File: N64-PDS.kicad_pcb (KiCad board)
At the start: 2 copper layers, 36 x 59.8 mm, 40 parts, among them J1 PWR_OUT, J2 I2C_OUT, J3 USB-C-6P-PWR, U1 ST1S41PHR, U2 ST1S41PHR, U3 STL6P3LLH6, U4 STUSB4500QTR

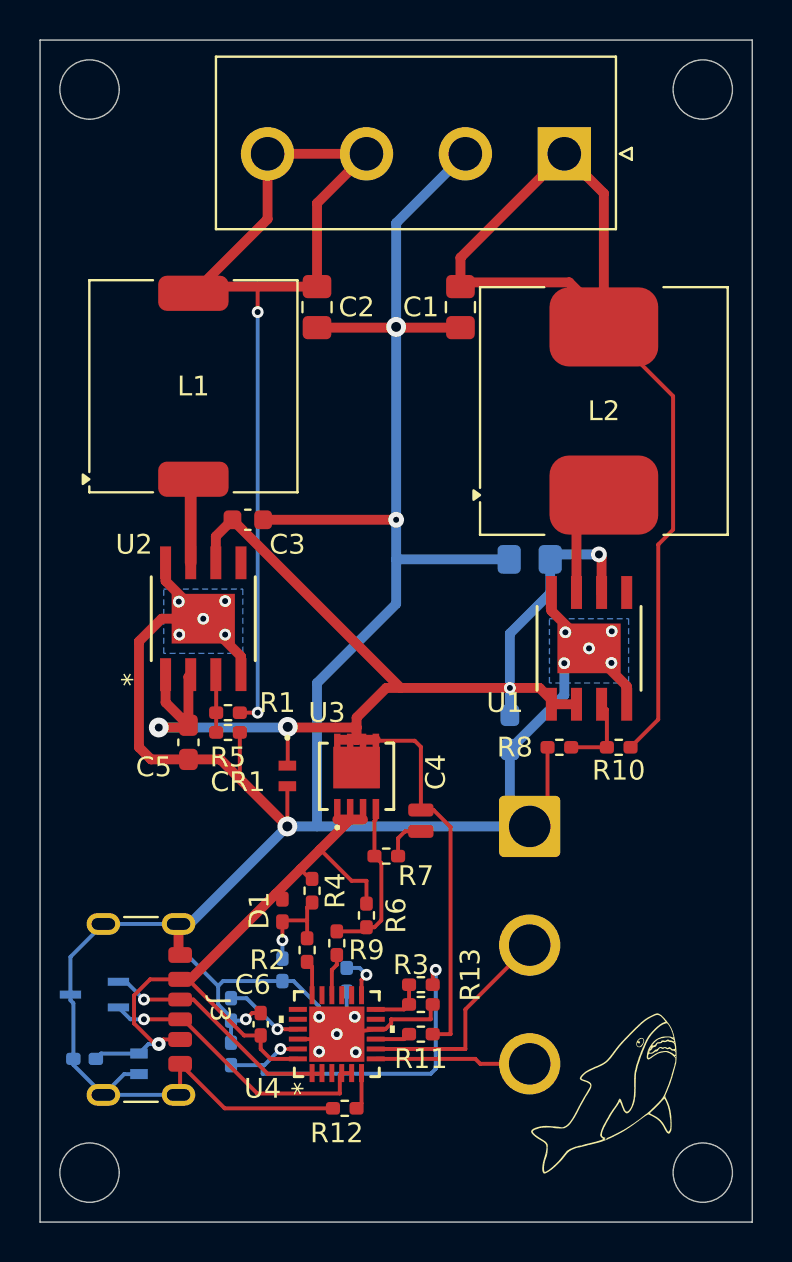
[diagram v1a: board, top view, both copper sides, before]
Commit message: Update PCB
slight reshuffle of the PCB in the aim of reducing noise from smps
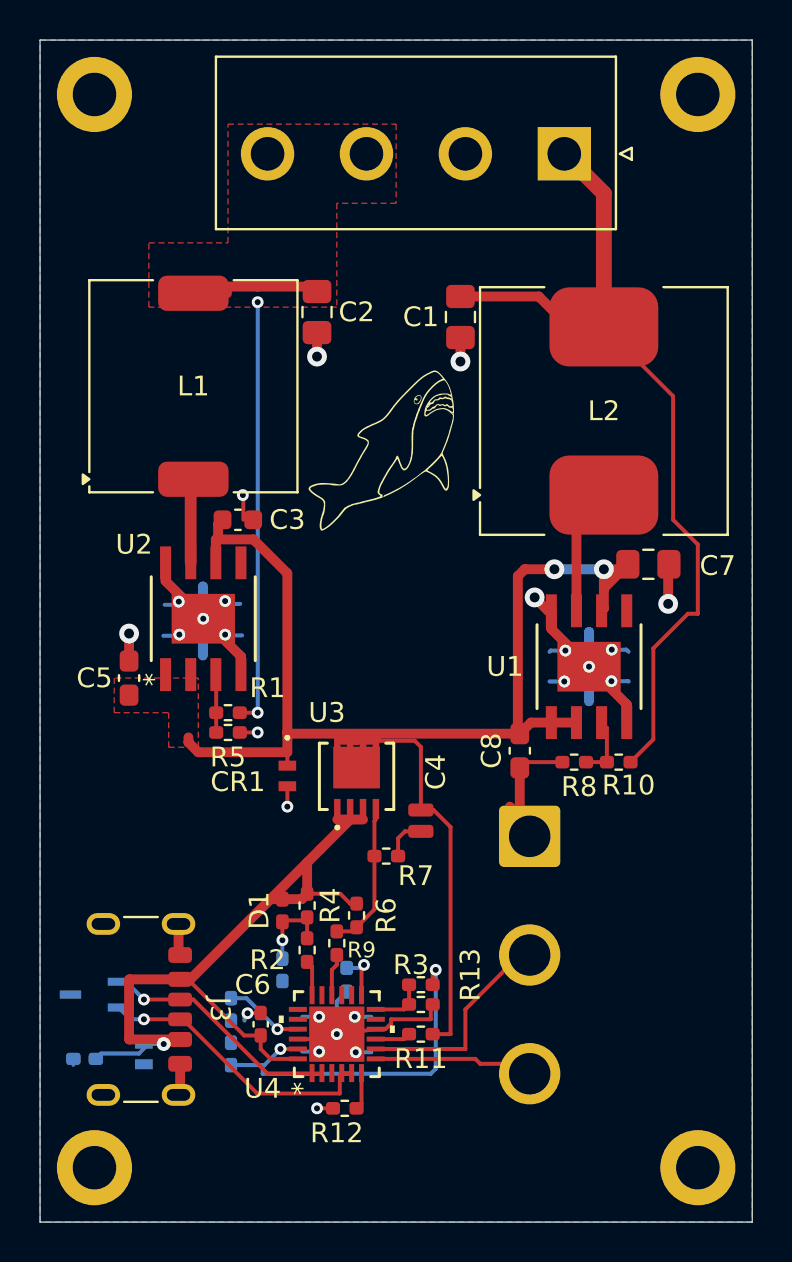
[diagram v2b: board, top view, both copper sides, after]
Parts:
- added REF**: MountingHole_2.2mm_M2_DIN965_Pad, MountingHole:MountingHole_2.2mm_M2_DIN965_Pad, F.Cu at (166.8, 68.5)
- added REF**: MountingHole_2.2mm_M2_DIN965_Pad, MountingHole:MountingHole_2.2mm_M2_DIN965_Pad, F.Cu at (166.8, 122.8)
- added REF**: MountingHole_2.2mm_M2_DIN965_Pad, MountingHole:MountingHole_2.2mm_M2_DIN965_Pad, F.Cu at (136.2, 122.8)
- added REF**: MountingHole_2.2mm_M2_DIN965_Pad, MountingHole:MountingHole_2.2mm_M2_DIN965_Pad, F.Cu at (136.2, 68.5)
- C7, C8: moved to F.Cu
- moved G*** 34.4 mm to (150.8, 86.5)
- moved C7 6.01 mm to (164.2, 92.2), turned to 0 degrees
- moved C5 4.42 mm to (138.0, 98.0), turned to -90 degrees
- moved R8 1.06 mm to (160.5, 102.2)
- moved C8 1.05 mm to (157.8, 101.7)
- moved U1 0.92 mm to (161.2, 97.4)
- moved R4 0.79 mm to (147.0, 109.5)
- moved R10 0.75 mm to (162.8, 102.2)
- moved CR3 0.56 mm to (138.8, 117.0)
- moved C1 0.50 mm to (154.8, 79.8)
- moved C3 0.50 mm to (143.5, 90.0)
- moved J2 0.50 mm to (158.2, 106.0)
- moved R6 0.50 mm to (149.5, 110.0)
- moved C2 0.25 mm to (147.5, 79.5)
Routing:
- net GND: track 183.3 -> 65.3 mm, vias 19 -> 25
- net 3V3O: track 49.7 -> 29.3 mm
- net 12VO: track 49.8 -> 41.4 mm
- net VSNK: track 81.8 -> 75.8 mm, vias 4 -> 2
- net /VBUS: track 36.5 -> 40.0 mm
- net /12V_SWO: track 3.54 -> 5.92 mm
- net /VBUS_VS_DISCH: track 4.95 -> 3.94 mm
- net 12VFB: track 4.09 -> 3.17 mm
- net Net-(U3-G): track 7.46 -> 6.94 mm
- added copper zone on F.Cu, net 3V3O
- added copper zone on F.Cu, net VSNK
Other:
- outline, holes or cut-outs redrawn

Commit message: Re-route
Re-route to improve design, further updates to come
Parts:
- C10, C11, CR2, CR3: moved to F.Cu
- C12: footprint Capacitor_SMD:C_0402_1005Metric_Pad0.74x0.62mm_HandSolder -> Capacitor_SMD:C_0805_2012Metric_Pad1.18x1.45mm_HandSolder; moved to F.Cu
- moved C12 12.0 mm to (144.5, 109.0)
- moved CR2 8.03 mm to (144.2, 115.0), turned to 0 degrees
- moved CR3 7.28 mm to (143.5, 111.5), turned to 90 degrees
- moved J2 6.75 mm to (165.0, 106.0)
- moved R12 5.25 mm to (154.0, 121.0), turned to 90 degrees
- moved C11 5.01 mm to (148.0, 116.0), turned to 180 degrees
- moved C10 4.85 mm to (148.0, 117.0), turned to 180 degrees
- moved C6 4.53 mm to (148.4, 118.0), turned to 180 degrees
- moved C9 4.09 mm to (149.8, 113.6)
- moved D1 4.09 mm to (149.8, 110.6)
- moved R11 4.09 mm to (156.8, 116.8)
- moved R13 4.09 mm to (156.8, 115.3)
- moved R14 4.09 mm to (153.0, 114.1)
- moved R2 4.09 mm to (151.0, 112.6)
- moved R3 4.09 mm to (156.8, 114.3)
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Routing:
- net GND: track 65.3 -> 86.4 mm, vias 25 -> 26
- net 2V7: track 18.8 -> 12.7 mm
- net /VBUS: track 40.0 -> 43.0 mm, vias 1 -> 2
- net /I2C_SDA: track 11.1 -> 14.0 mm
- net Net-(U3-G): track 6.94 -> 9.77 mm
- net Net-(J3-CC1): track 11.8 -> 14.6 mm, vias 1 -> 2
- net /I2C_SCL: track 7.89 -> 10.6 mm
- net VSNK: track 75.8 -> 78.4 mm
- net Net-(J3-CC2): track 14.4 -> 16.7 mm, vias 1 -> 2
- net Net-(U4-VREG_1V2): track 4.03 -> 2.21 mm, vias 1 -> 0
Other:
- board size 36 x 59.8 mm -> 35.5 x 59.8 mm

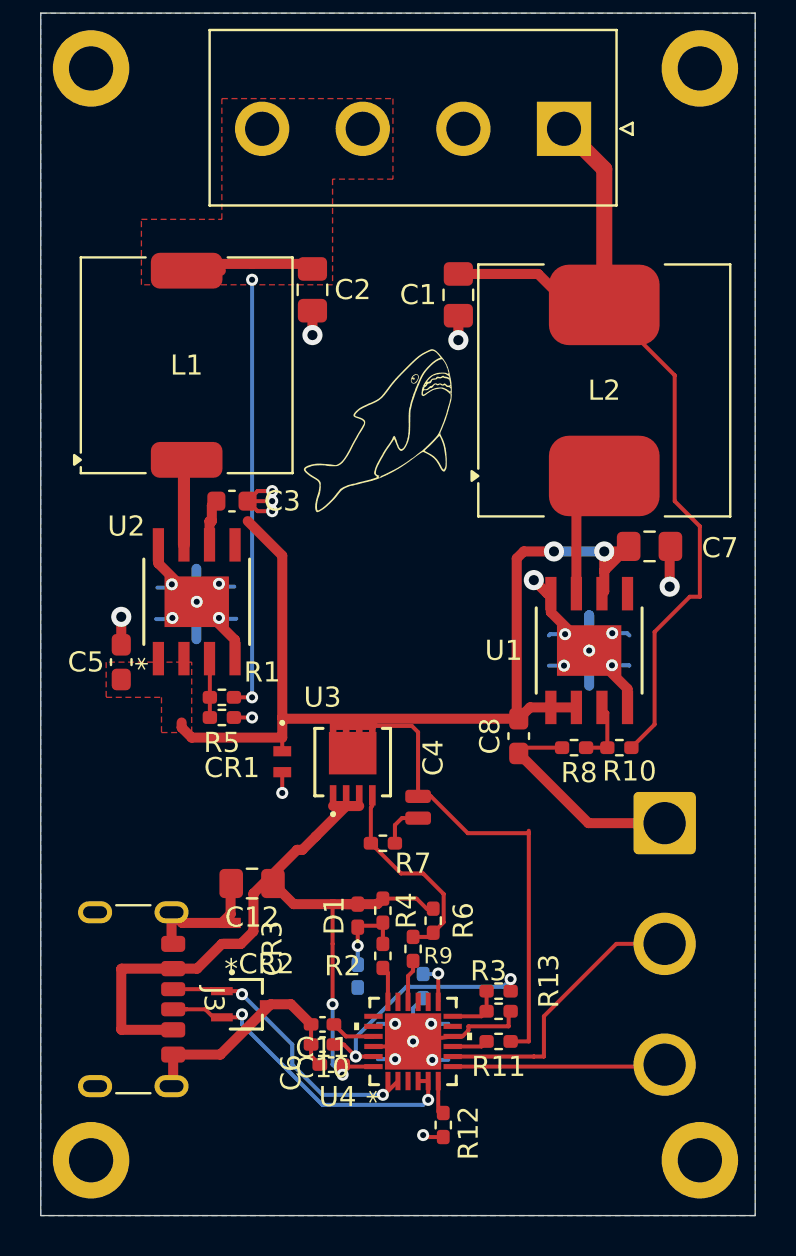
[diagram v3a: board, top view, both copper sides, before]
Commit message: 4Layer
4 layer board, destroy 12v rail to make space for new 12v rail.
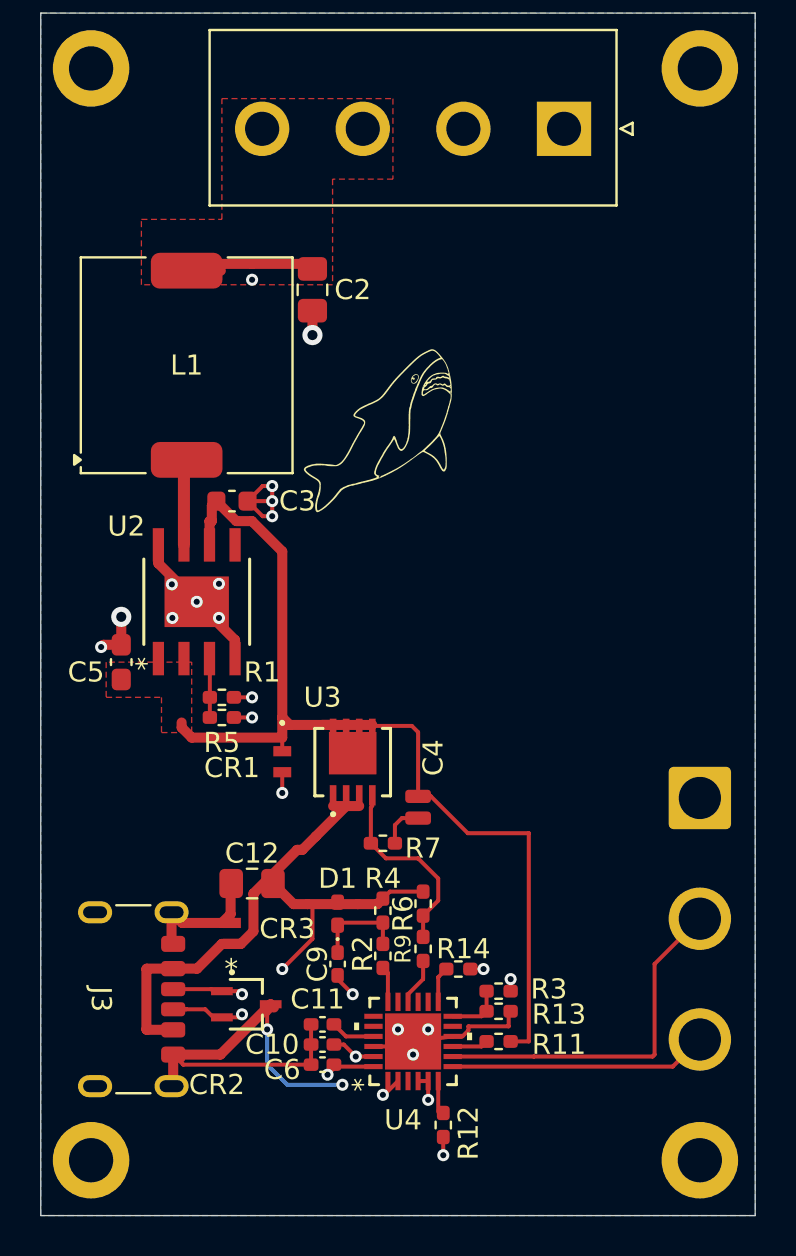
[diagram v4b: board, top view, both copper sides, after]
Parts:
- removed C1, C7: 10u, Capacitor_SMD:C_0805_2012Metric_Pad1.18x1.45mm_HandSolder
- removed C8: 10u, Capacitor_SMD:C_0603_1608Metric_Pad1.08x0.95mm_HandSolder
- removed L2: 10u, Inductor_SMD:L_Coilcraft_MSS1260-XXX
- removed R10: 180k, Resistor_SMD:R_0402_1005Metric_Pad0.72x0.64mm_HandSolder
- removed R8: 13k, Resistor_SMD:R_0402_1005Metric_Pad0.72x0.64mm_HandSolder
- removed U1: ST1S41PHR, ST1S41PHR:HSOP8_STM-M
- C9, R14: moved to F.Cu
- moved J2 2.15 mm to (166.8, 104.8)
- moved R14 1.94 mm to (154.8, 113.2), turned to 0 degrees
- moved C9 1.16 mm to (148.8, 113.0)
- moved D1 1.00 mm to (148.8, 110.5)
- moved R6 0.98 mm to (153.0, 110.0)
- moved R9 0.50 mm to (153.0, 112.2)
- moved C6 0.43 mm to (148.0, 118.0)
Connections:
- REF** pad 1: (no net) -> GND
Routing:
- net 12VO: track 41.4 -> 0.00 mm
- net VSNK: track 78.4 -> 50.4 mm, vias 2 -> 0
- net GND: track 86.4 -> 58.7 mm, vias 26 -> 21
- net /12V_SWO: track 5.92 -> 0.00 mm
- net /I2C_SDA: track 14.0 -> 17.8 mm
- net 12VFB: track 3.17 -> 0.00 mm
- net /I2C_SCL: track 10.6 -> 12.8 mm
- net /VBUS: track 43.0 -> 41.4 mm
- net Net-(J3-CC1): track 14.6 -> 15.7 mm
- net Net-(J3-CC2): track 16.7 -> 17.9 mm
- net /VBUS_VS_DISCH: track 3.94 -> 4.57 mm, vias 1 -> 0
- net Net-(U3-G): track 9.77 -> 9.16 mm
- net /ADDR1: track 2.17 -> 1.80 mm, vias 1 -> 0
- added copper zone on In1.Cu, net GND
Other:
- copper layers 2 -> 4

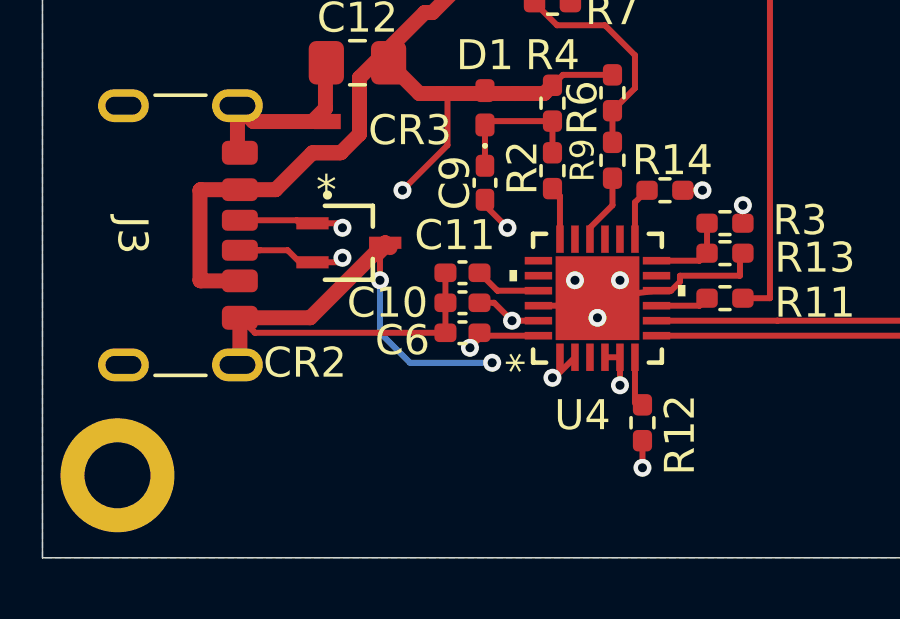
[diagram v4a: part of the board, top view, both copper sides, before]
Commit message: Component switch
Switch buck/boost converter components, Complete schematic
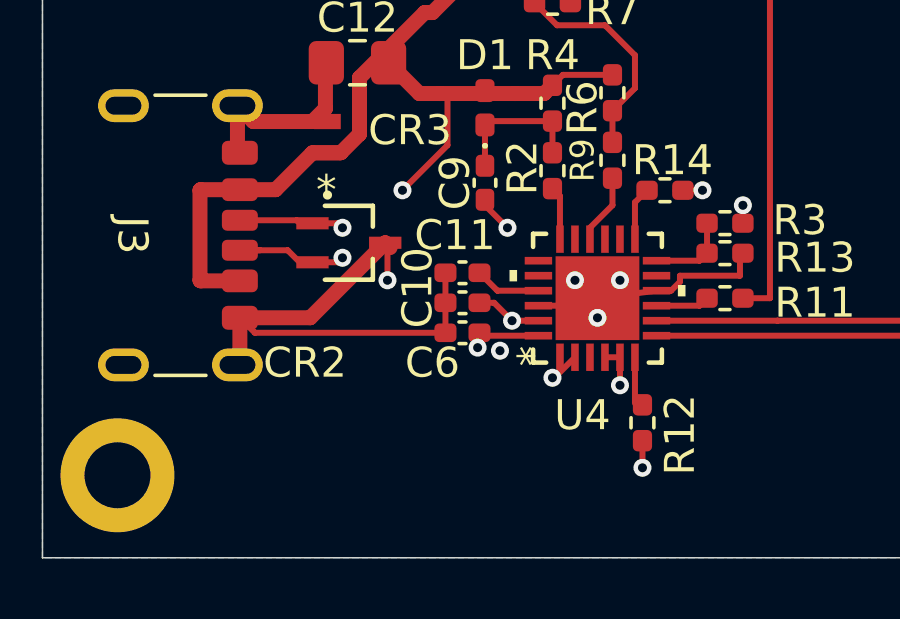
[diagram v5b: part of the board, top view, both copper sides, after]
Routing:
- net GND: track 58.7 -> 59.9 mm
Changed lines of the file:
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@@
 		(tags "capacitor handsolder")
 		(property "Reference" "C10"
-			(at 2.5 0 0)
+			(at 1.5 0.5 90)
 			(layer "F.SilkS")
 			(effects
@@
 		(tags "capacitor handsolder")
 		(property "Reference" "C6"
-			(at 2 -0.25 180)
+			(at 1 -1 180)
 			(layer "F.SilkS")
 			(effects
@@
 		)
 		(fp_text user "*"
-			(at -2.1525 -2.5 90)
+			(at -1.92802 -2.1463 90)
 			(unlocked yes)
 			(layer "F.SilkS")
@@
 	)
 	(segment
-		(start 148.5675 118.1825)
-		(end 148.25 118.5)
-		(width 0.2)
-		(layer "F.Cu")
-		(net 2)
-	)
-	(segment
 		(start 151 109.75)
 		(end 150.725 110.025)
@@
 	)
 	(segment
-		(start 148.5675 118)
-		(end 148.5675 118.1825)
-		(width 0.2)
-		(layer "F.Cu")
-		(net 2)
-	)
-	(segment
 		(start 149.75 110.025)
 		(end 148.5 110.025)
@@
 	)
 	(segment
+		(start 148.505232 118.494923)
+		(end 148.5675 118.432655)
+		(width 0.2)
+		(layer "F.Cu")
+		(net 2)
+	)
+	(segment
 		(start 147 107.325998)
 		(end 146.741502 107.325998)
@@
 	)
 	(segment
+		(start 148.5675 118.432655)
+		(end 148.5675 118)
+		(width 0.2)
+		(layer "F.Cu")
+		(net 2)
+	)
+	(segment
 		(start 147.662999 106.662999)
 		(end 149.174999 105.151)
@@
 	)
 	(via
-		(at 148.25 118.5)
+		(at 148.505232 118.494923)
 		(size 0.6)
 		(drill 0.3)
@@
 	)
 	(segment
-		(start 147.5 117.75)
-		(end 147.5 114.75)
+		(start 147.5 114.75)
+		(end 146 113.25)
 		(width 0.2)
 		(layer "In2.Cu")
@@
 	)
 	(segment
-		(start 148.25 118.5)
-		(end 147.5 117.75)
+		(start 148.505232 118.494923)
+		(end 147.5 117.489691)
 		(width 0.2)
 		(layer "In2.Cu")
@@
 	)
 	(segment
-		(start 147.5 114.75)
-		(end 146 113.25)
+		(start 147.5 117.489691)
+		(end 147.5 114.75)
 		(width 0.2)
 		(layer "In2.Cu")
@@
 	)
 	(segment
+		(start 142.9257 117.5)
+		(end 140.58 117.5)
+		(width 0.5)
+		(layer "F.Cu")
+		(net 3)
+	)
+	(segment
 		(start 140.5 110.43)
 		(end 140.5 111.92)
@@
 	)
 	(segment
-		(start 145.25 115.5)
-		(end 145.25 116.25)
+		(start 145.5 115.25)
+		(end 145.58785 115.16215)
 		(width 0.2)
 		(layer "F.Cu")
@@
 	)
 	(segment
-		(start 145.4257 115)
-		(end 142.9257 117.5)
-		(width 0.5)
-		(layer "F.Cu")
-		(net 3)
-	)
-	(segment
 		(start 145.5 89.25)
 		(end 145.5 90.75)
@@
 	)
 	(segment
-		(start 145.58785 115.16215)
-		(end 145.25 115.5)
+		(start 145.4257 115)
+		(end 142.9257 117.5)
+		(width 0.5)
+		(layer "F.Cu")
+		(net 3)
+	)
+	(segment
+		(start 145.5 116.25)
+		(end 145.5 115.25)
 		(width 0.2)
 		(layer "F.Cu")
@@
 	)
 	(segment
-		(start 142.9257 117.5)
-		(end 140.58 117.5)
-		(width 0.5)
-		(layer "F.Cu")
-		(net 3)
-	)
-	(segment
 		(start 154.4685 116.5975)
 		(end 152.5 116.8475)
@@
 	)
 	(via
-		(at 145.25 116.25)
+		(at 145.5 116.25)
 		(size 0.6)
 		(drill 0.3)
@@
 	)
 	(via
-		(at 148.989897 119)
+		(at 149.25 118.5975)
 		(size 0.6)
 		(drill 0.3)
@@
 	)
 	(segment
-		(start 148.989897 119)
-		(end 146.25 119)
+		(start 144.8 116.95)
+		(end 145.5 116.25)
 		(width 0.2)
-		(layer "B.Cu")
+		(layer "In2.Cu")
 		(net 3)
 	)
 	(segment
-		(start 145.25 118)
-		(end 145.25 116.25)
+		(start 149.25 118.5975)
+		(end 148.6475 119.2)
 		(width 0.2)
-		(layer "B.Cu")
+		(layer "In2.Cu")
 		(net 3)
 	)
 	(segment
-		(start 146.25 119)
-		(end 145.25 118)
+		(start 146.124264 119.2)
+		(end 144.8 117.875736)
 		(width 0.2)
-		(layer "B.Cu")
+		(layer "In2.Cu")
+		(net 3)
+	)
+	(segment
+		(start 144.8 117.875736)
+		(end 144.8 116.95)
+		(width 0.2)
+		(layer "In2.Cu")
+		(net 3)
+	)
+	(segment
+		(start 148.6475 119.2)
+		(end 146.124264 119.2)
+		(width 0.2)
+		(layer "In2.Cu")
 		(net 3)
 	)
